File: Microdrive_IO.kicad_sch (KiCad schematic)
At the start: 10 parts

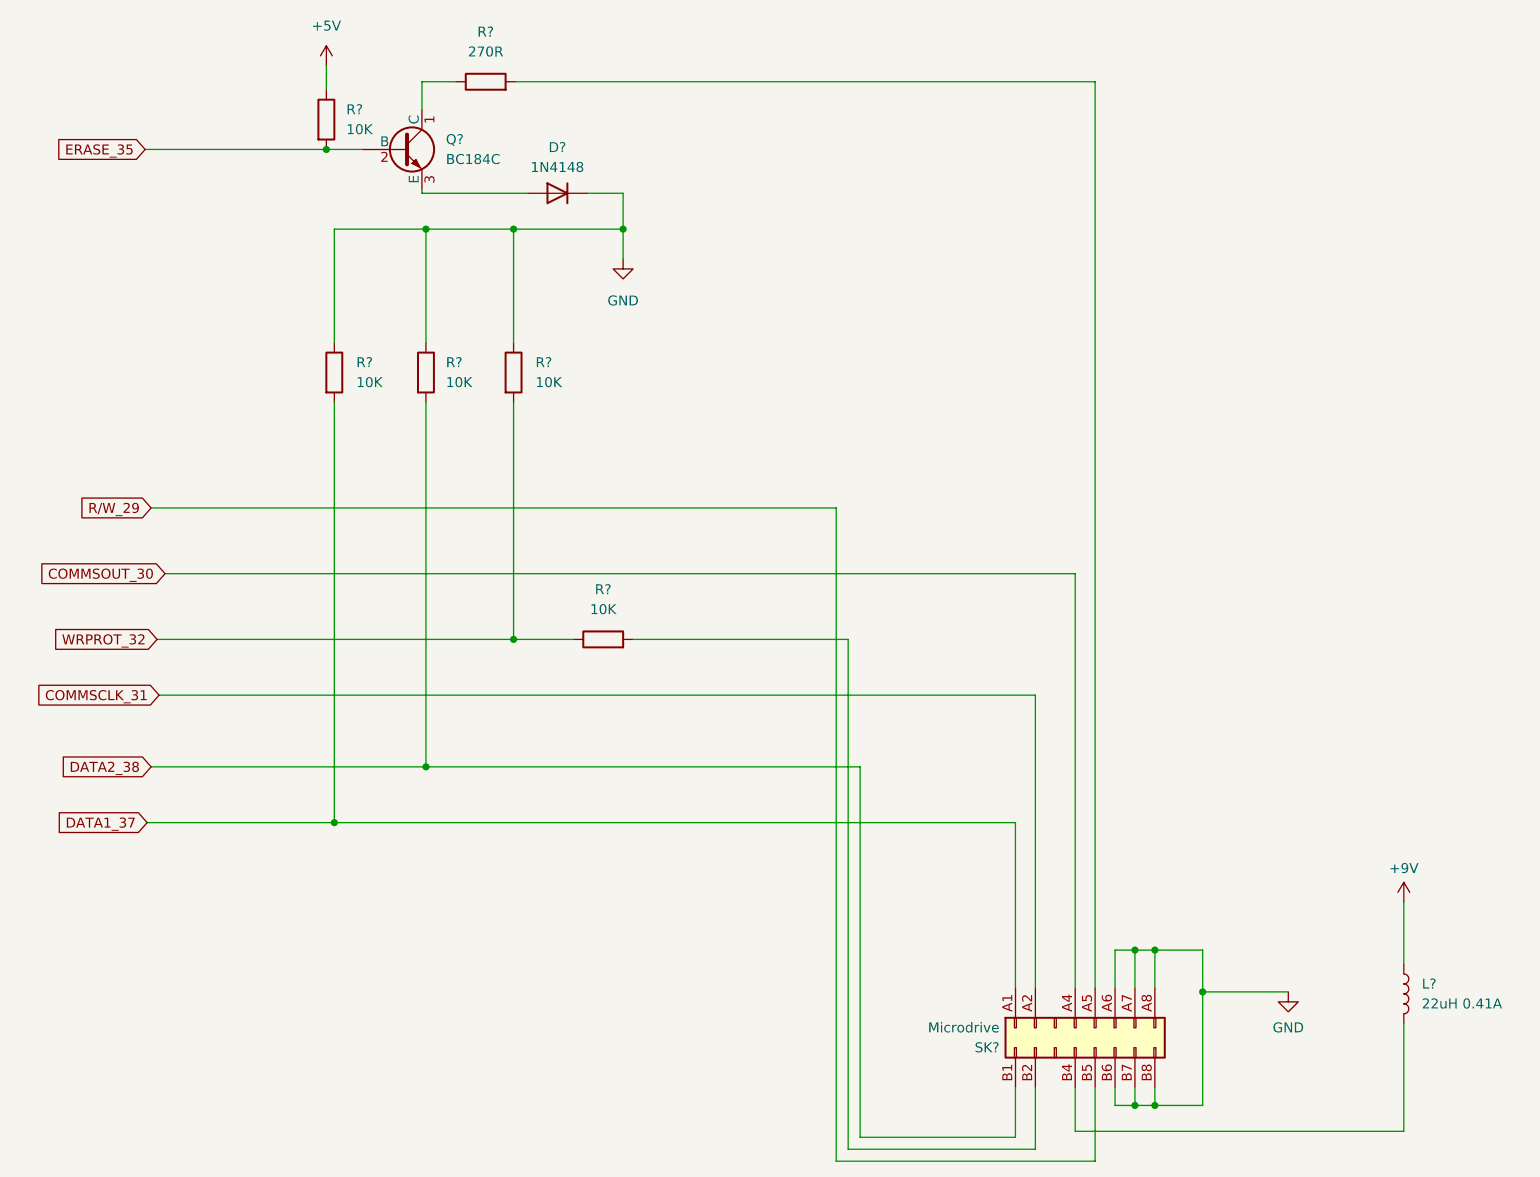
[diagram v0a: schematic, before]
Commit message: Add files via upload
Updated with Kicad 9. Now includes bom/ibom.html (Interactice BOM)
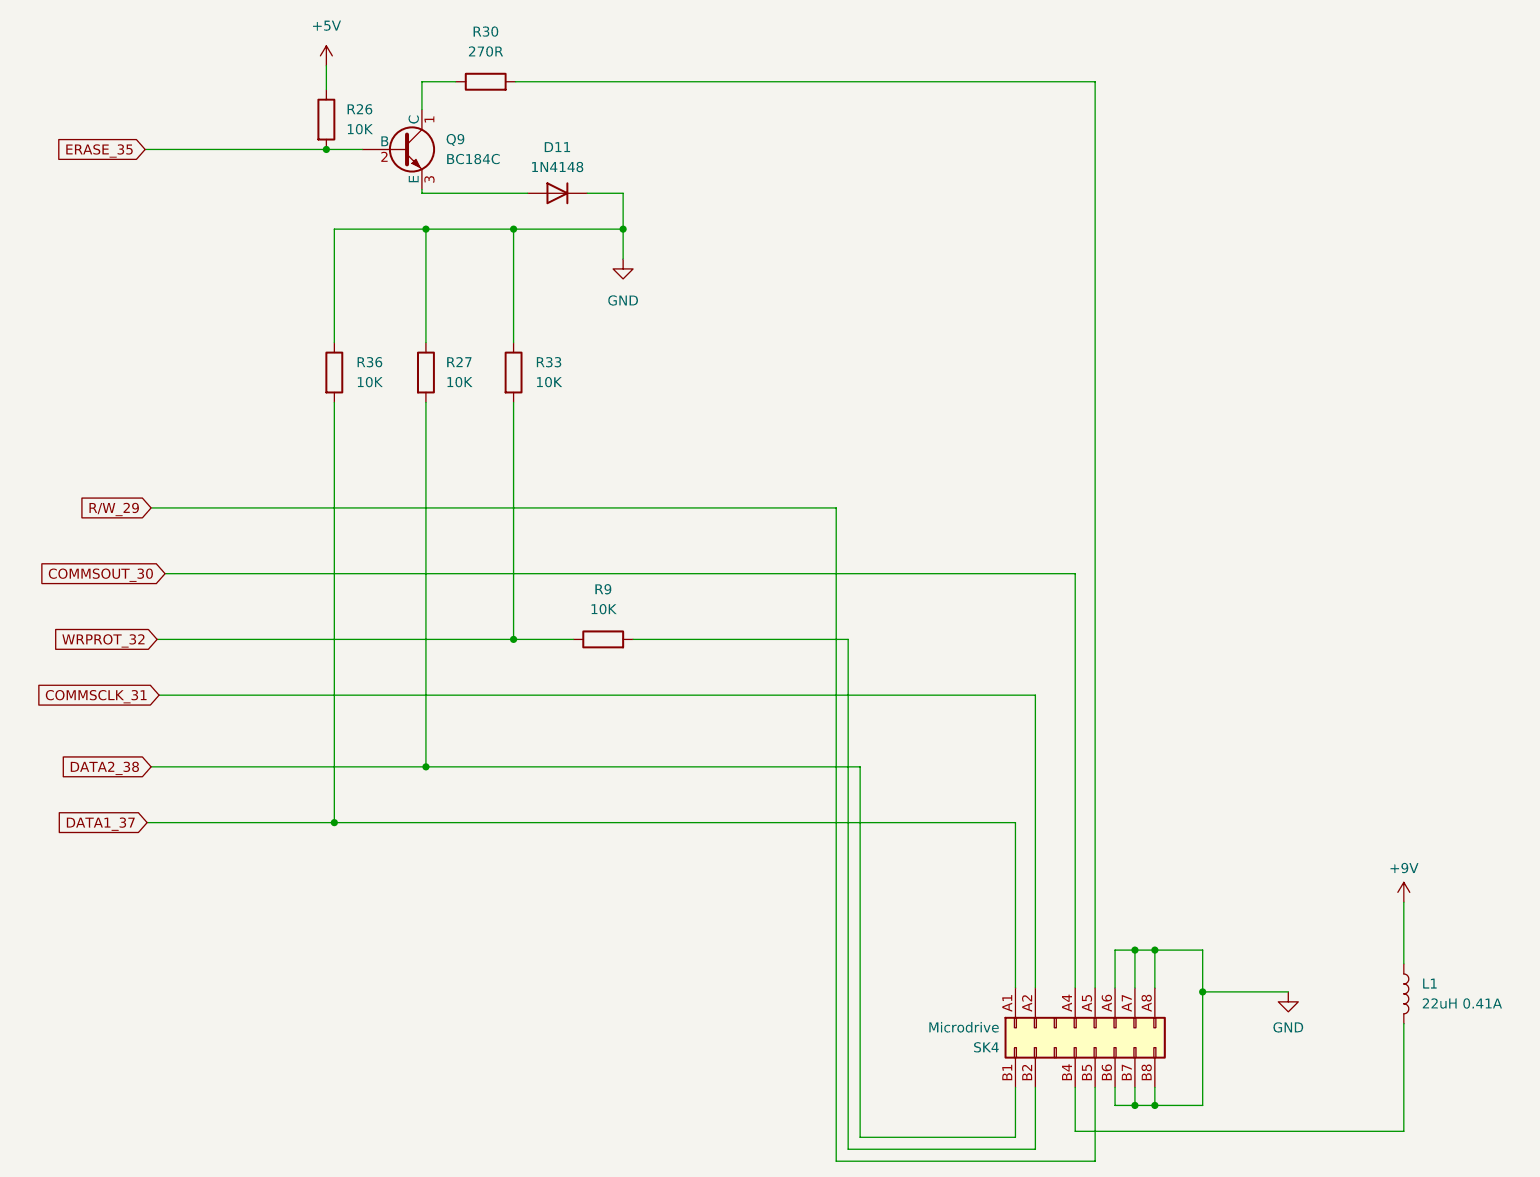
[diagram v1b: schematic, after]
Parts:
- D11: renamed from D?; footprint Spectrum:Diode 1N -> Mod:Diode 1N
- L1: renamed from L?; footprint Inductor_THT:L_Axial_L12.8mm_D5.8mm_P20.32mm_Horizontal_Fastron_HBCC -> Mod:L_Axial_L12.8mm_D5.8mm_P20.32mm_Horizontal_Fastron_HBCC
- Q9: renamed from Q?; footprint Package_TO_SOT_THT:TO-92L_Inline_Wide -> Mod:TO-92L_Inline_Wide
- R26, R27, R30, R33, R36, R9: renamed from R?; footprint Spectrum:Resistor_0.25W -> Mod:Resistor_0.25W
- SK4: renamed from SK?; footprint ZX Bits:ZX_MD_Edge_Connector -> Mod:ZX_MD_Edge_Connector; symbol ZX_IF1_MD:ZX_Spectrum_MD_Connector -> IF1_Symbols:ZX_Spectrum_MD_Connector
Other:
- company: (none) -> Drawn by liveboxandy
- title: ZX Interface 1 Schematic -> ZX Interface 1 Schematic - Sinclair Labels
